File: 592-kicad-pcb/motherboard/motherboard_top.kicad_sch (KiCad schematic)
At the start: 32 parts, among them J21 Conn_02x01, J22 Conn_02x01, J23 Conn_02x01, J24 Conn_02x01, J25 Conn_02x01, J26 Conn_02x01, J5 Conn_01x04, U15 SN74LVC1G14DBV, U16 SN74LVC1G00DCK, U17 74CBTLV3257PW,118, U18 SN74LVC1G14DBV, U19 74CBTLV3257PW,118, U20 74CBTLV3257PW,118, U21 74CBTLV3257PW,118

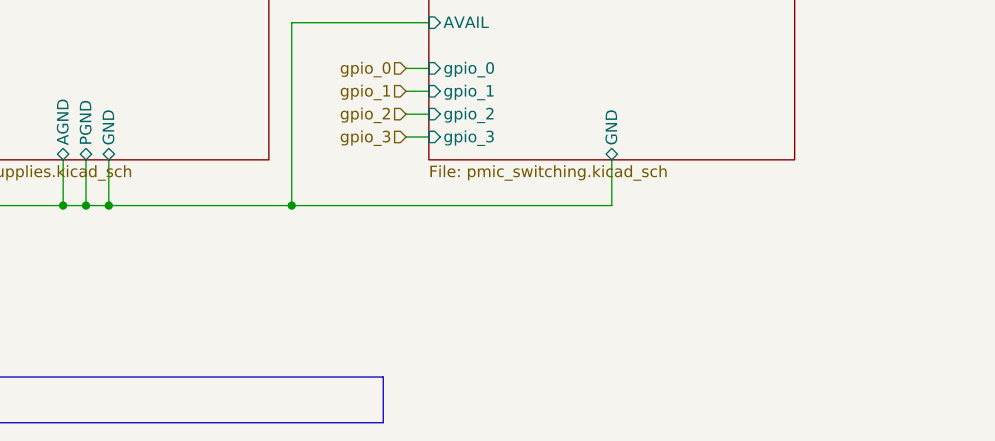
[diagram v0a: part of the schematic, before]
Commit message: need to map mthrbrd to nucleo + doc online
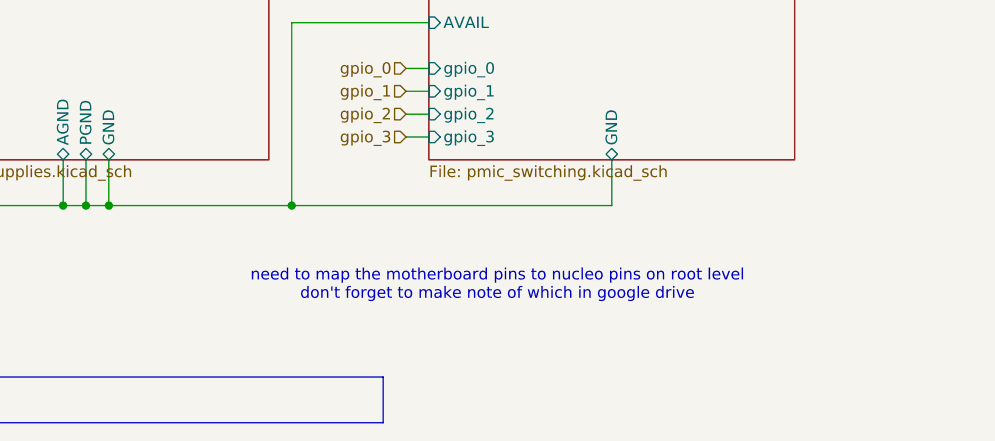
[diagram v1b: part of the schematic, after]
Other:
- note added: "need to map the motherboard pins to nucleo pins on root level don't forget to make note of which in google drive"
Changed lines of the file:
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@@
+		)
+	)
+	(text "need to map the motherboard pins to nucleo pins on root level\ndon't forget to make note of which in google drive"
+		(exclude_from_sim no)
+		(at 157.48 389.89 0)
+		(effects
+			(font
+				(size 1.27 1.27)
+			)
 		)
 	)

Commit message: will it conflict?
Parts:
- removed J21, J22, J23, J24, J25, J26: Conn_02x01, Connector_PinHeader_1.27mm:PinHeader_1x02_P1.27mm_Vertical, symbol Connector_Generic:Conn_02x01
- removed J5: Conn_01x04, symbol Connector_Generic:Conn_01x04
- added U33, U34: SMXS-04K, 592-partslib:SMXS-04K-TP, symbol 592-partslib:SMXS-04K
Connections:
- net GND: now also U33.1 (1i), U33.2 (2i), U33.3 (3i), U33.4 (4i), U34.1 (1i), U34.2 (2i), U34.3 (3i), U34.4 (4i)
- net GPIO_JTAG_FTDI_source_select: now also U33.7 (2o)
- net GPIO_MGMT_enable: now also U33.8 (1o)
- net GPIO_SPI_MGMT_source_sel: now also U34.5 (4o)
- net GPIO_ftdi_jtag_src_en: now also U33.6 (3o)
- net GPIO_rck_mem_sel_sdB: now also U34.8 (1o)
- net GPIO_rck_mem_source_en: now also U34.6 (3o)
- net GPIO_rck_mem_source_sel_ftdiB: now also U34.7 (2o)
- net chip_spi_flash_0_cs_0: now also U17.13; no longer U20.6
- net chip_spi_flash_0_dq_0: now also U20.10; no longer U20.3
- net chip_spi_flash_0_dq_1: now also U20.13; no longer U20.10
- net chip_spi_flash_0_dq_2: now also U20.3; no longer U17.6
- net chip_spi_flash_0_dq_3: now also U20.6; no longer U17.3
- net chip_spi_flash_0_sck: now also U17.10; no longer U20.13
- net ftdi_spi_cs: now also U17.14; no longer U20.5
- net ftdi_spi_miso: now also U20.14; no longer U20.11
- net ftdi_spi_mosi: now also U20.11; no longer U20.2
- net ftdi_spi_sck: now also U17.11; no longer U20.14
- net rck_mem_cs: now also U17.12; no longer U20.7
- net rck_mem_io2: now also U20.4; no longer U17.7
- net rck_mem_io3: now also U20.7; no longer U17.4
- net rck_mem_miso_i01: now also U20.12; no longer U20.9
- net rck_mem_mosi_io0: now also U20.9; no longer U20.4
- net rck_mem_sck: now also U17.9; no longer U20.12
- net at R58.2: now also U20.2; no longer U17.5
- net at U17.2: no longer R57.2
- new net: R57.2, U20.5
- no-connect marks 7 -> 9
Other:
- sheet pmic_supplies ports: added none; removed 1V8, 1V8_EXT_IN, 2V5, 2V5_EXT_IN, 3V3, 3V3_EXT_IN, 5V0_ON_BOARD, AGND, GND, PG, PGND
- sheet pmic_switching ports: added none; removed 1V8, 2V5, 3V3, 5V0_ON_BOARD, AVAIL, GND, VCCD, VCCD1, VCCD2, VDDA, VDDIO, VDDA1, VDD_EXT, dig_to_adc, gpio_0, gpio_1, gpio_2, gpio_3, ldo_to_adc
- note removed: "need to map the motherboard pins to nucleo pins on root level don't forget to make note of which in google drive"
- moved on the sheet: R57, R58

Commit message: check in
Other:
- sheet pmic_supplies ports: added 1V8, 1V8_EXT_IN, 2V5, 2V5_EXT_IN, 3V3, 3V3_EXT_IN, 5V0_ON_BOARD, AGND, GND, PG, PGND; removed none
- sheet pmic_switching ports: added 1V8, 2V5, 3V3, 5V0_ON_BOARD, AVAIL, GND, VCCD, VCCD1, VCCD2, VDDA, VDDIO, VDDA1, VDDA2, VDD_EXT, dig_to_adc, gpio_0, gpio_1, gpio_2, gpio_3, ldo_to_adc; removed none

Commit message: no erc errors but on root
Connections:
- no-connect marks 9 -> 8
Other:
- sheet pmic_switching ports: added none; removed AVAIL, gpio_3
- moved on the sheet: R98, R99, U17A, U17B, U17C, U17D, U17E, U33, U34
